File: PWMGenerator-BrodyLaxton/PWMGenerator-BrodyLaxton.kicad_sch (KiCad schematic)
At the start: 30 parts, among them J1 Conn_01x03_Pin, Q1 2N3904, Q2 2N3904, Q3 2N3906, Q4 2N3906, SW2 SW_SPST, U1 LM339, U2 LM7805_TO220

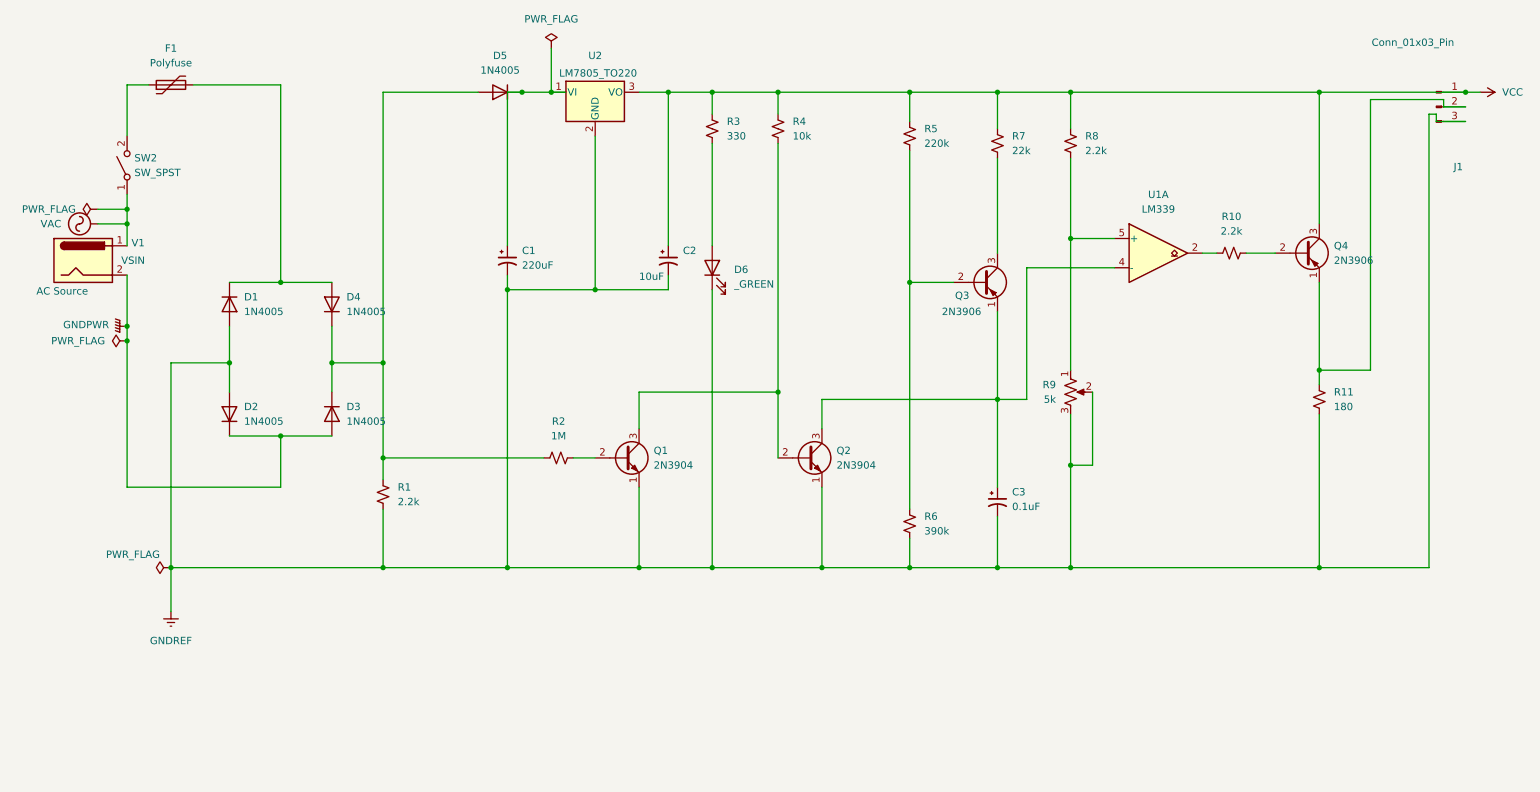
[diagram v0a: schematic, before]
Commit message: project2 updated
had to update the polyfuse sylmbol
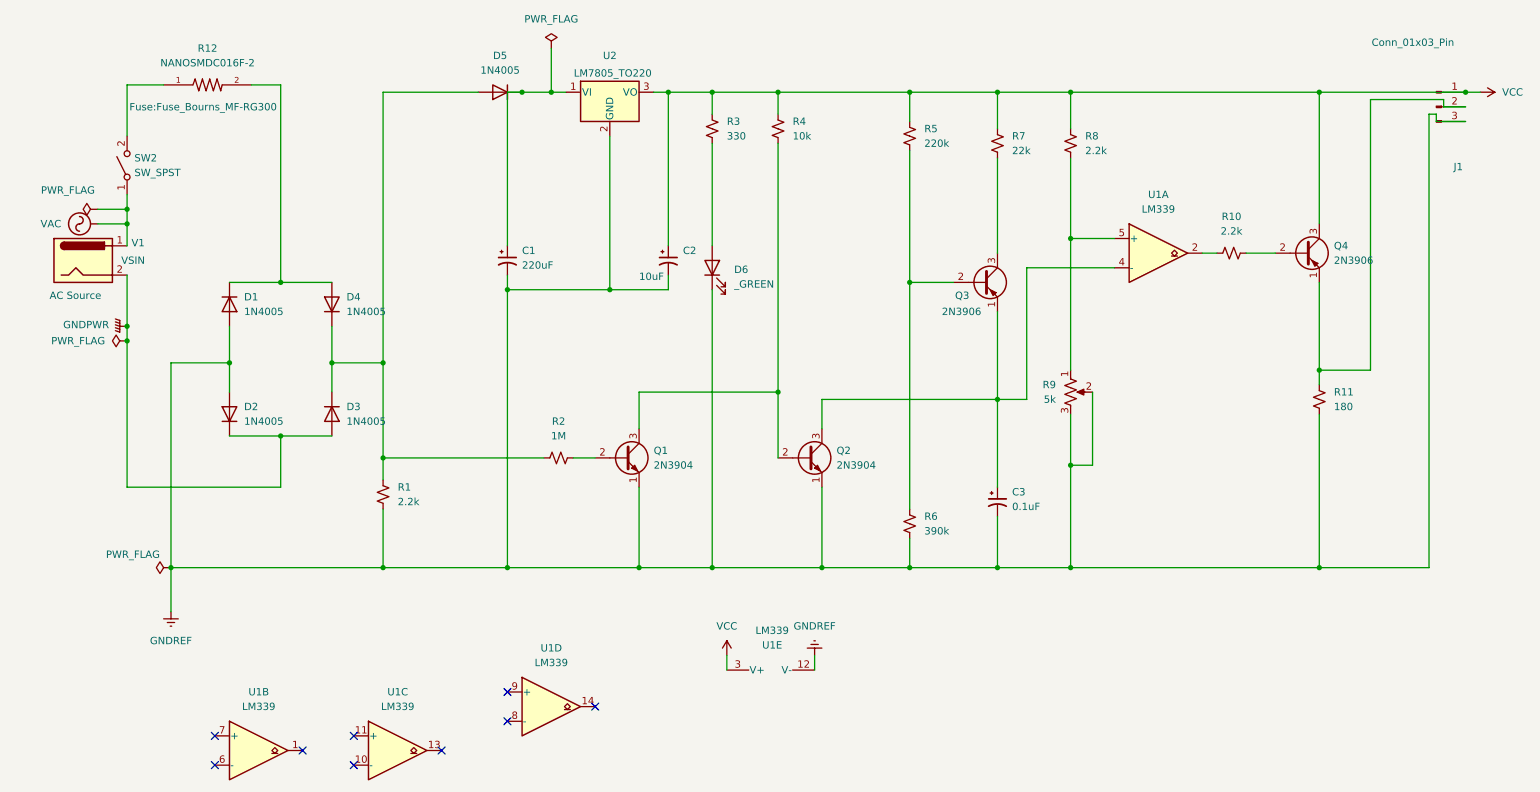
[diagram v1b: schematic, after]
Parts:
- removed F1: Polyfuse, Fuse:Fuse_Bourns_MF-SM_7.98x5.44mm, symbol Device:Polyfuse
- added R12: NANOSMDC016F-2, Fuse:Fuse_Bourns_MF-RG300, symbol NANOSMDC016F-2:NANOSMDC016F-2
- added unit 2 of U1
- added unit 4 of U1
- added unit 3 of U1
- added unit 5 of U1
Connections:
- net GNDREF: now also U1.12 (V-)
- net VCC: now also U1.3 (V+)
- net at D1.1 (K), D4.2 (A): now also R12.2
- net at SW2.2 (B): now also R12.1
- no-connect marks 0 -> 9
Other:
- moved on the sheet: U2

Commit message: project 3
part 2 done
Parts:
- R11: footprint (none) -> Resistor_SMD:R_0805_2012Metric
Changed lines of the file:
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@@
 			)
 		)
-		(property "Footprint" ""
+		(property "Footprint" "Resistor_SMD:R_0805_2012Metric"
 			(at 234.95 116.84 0)
 			(effects
@@
 			)
 		)
-		(property "Datasheet" "~"
+		(property "Datasheet" "https://www.digikey.ca/en/products/detail/littelfuse-inc/NANOSMDC016F-2/1040822?s=N4IgTCBcDaIHIEE4HkDKBZAIgYQAwEYA2AMQFoIBdAXyA"
 			(at 234.95 116.84 0)
 			(effects

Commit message: part 4
part 4 complete
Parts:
- removed V1: VSIN, Connector_BarrelJack:BarrelJack_SwitchcraftConxall_RAPC10U_Horizontal, symbol Connector:Barrel_Jack
- added J2: Barrel_Jack_MountingPin, Connector_BarrelJack:BarrelJack_Wuerth_694106106102_2.0x5.5mm, symbol Connector:Barrel_Jack_MountingPin
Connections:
- net GNDPWR: now also J2.2
- net VAC: now also J2.1
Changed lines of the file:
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@@
 	(wire
 		(pts
+			(xy 25.4 90.17) (xy 27.94 90.17)
+		)
+		(stroke
+			(width 0)
+			(type default)
+		)
+	)
+	(wire
+		(pts
 			(xy 191.77 88.9) (xy 199.39 88.9)
 		)
@@
 	(wire
 		(pts
+			(xy 25.4 95.25) (xy 27.94 95.25)
+		)
+		(stroke
+			(width 0)
+			(type default)
+		)
+	)
+	(wire
+		(pts
 			(xy 93.98 63.5) (xy 93.98 90.17)
 		)
@@
 	)
 	(symbol
-		(lib_id "Connector:Barrel_Jack")
-		(at 20.32 92.71 0)
-		(unit 1)
-		(exclude_from_sim no)
-		(in_bom yes)
-		(on_board yes)
-		(dnp no)
-		(property "Reference" "V1"
-			(at 28.702 89.662 0)
-			(effects
-				(font
-					(size 1.27 1.27)
-				)
-				(justify left)
-			)
-		)
-		(property "Value" "VSIN"
-			(at 26.924 92.71 0)
-			(effects
-				(font
-					(size 1.27 1.27)
-				)
-				(justify left)
-			)
-		)
-		(property "Footprint" "Connector_BarrelJack:BarrelJack_SwitchcraftConxall_RAPC10U_Horizontal"
-			(at 21.59 93.726 0)
-			(effects
-				(font
-					(size 1.27 1.27)
-				)
-				(hide yes)
-			)
-		)
-		(property "Datasheet" "~"
-			(at 21.59 93.726 0)
-			(effects
-				(font
-					(size 1.27 1.27)
-				)
-				(hide yes)
-			)
-		)
-		(property "Description" "DC Barrel Jack"
-			(at 20.32 92.71 0)
-			(effects
-				(font
-					(size 1.27 1.27)
-				)
-				(hide yes)
-			)
-		)
-		(property "Sim.Pins" "1=+ 2=-"
-			(at 20.32 92.71 0)
-			(effects
-				(font
-					(size 1.27 1.27)
-				)
-				(hide yes)
-			)
-		)
-		(property "Sim.Params" "AC Source"
-			(at 14.478 98.806 0)
-			(effects
-				(font
-					(size 1.27 1.27)
-				)
-				(justify left)
-			)
-		)
-		(property "Sim.Type" "SIN"
-			(at 20.32 92.71 0)
-			(effects
-				(font
-					(size 1.27 1.27)
-				)
-				(hide yes)
-			)
-		)
-		(property "Sim.Device" "V"
-			(at 20.32 92.71 0)
-			(effects
-				(font
-					(size 1.27 1.27)
-				)
-				(justify left)
-				(hide yes)
-			)
-		)
-		(pin "2"
-		)
-		(pin "1"
-		)
-		(instances
-			(project ""
-				(path "/5b381b0a-72a0-4ae7-af61-8b2e25058da2"
-					(reference "V1")
-					(unit 1)
-				)
-			)
-		)
-	)
-	(symbol
 		(lib_id "Device:LED")
 		(at 129.54 93.98 90)
@@
 					(unit 1)
 				)
+			)
+		)
+	)
+	(symbol
+		(lib_id "Connector:Barrel_Jack_MountingPin")
+		(at 17.78 92.71 0)
+		(unit 1)
+		(exclude_from_sim no)
+		(in_bom yes)
+		(on_board yes)
+		(dnp no)
+		(property "Reference" "J2"
+			(at 17.78 83.82 0)
+			(effects
+				(font
+					(size 1.27 1.27)
+				)
+			)
+		)
+		(property "Value" "Barrel_Jack_MountingPin"
+			(at 36.576 91.948 0)
+			(effects
+				(font
+					(size 1.27 1.27)
+				)
+			)
+		)
+		(property "Footprint" "Connector_BarrelJack:BarrelJack_Wuerth_694106106102_2.0x5.5mm"
+			(at 19.05 93.726 0)
+			(effects
+				(font
+					(size 1.27 1.27)
+				)
+				(hide yes)
+			)
+		)
+		(property "Datasheet" "~"
+			(at 19.05 93.726 0)
+			(effects
+				(font
+					(size 1.27 1.27)
+				)
+				(hide yes)
+			)
+		)
+		(property "Description" "DC Barrel Jack with a mounting pin"
+			(at 17.78 92.71 0)
+			(effects
+				(font
+					(size 1.27 1.27)
+				)
+				(hide yes)
+			)
+		)
+		(pin "2"
+		)
+		(pin "MP"
+		)
+		(pin "1"
+		)
+		(instances
+			(project ""
+				(path "/5b381b0a-72a0-4ae7-af61-8b2e25058da2"
+					(reference "J2")
+					(unit 1)
+				)
